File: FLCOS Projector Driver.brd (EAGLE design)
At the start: 73.9 x 62.1 mm, 65 parts, among them IC2 LM3414, IC3 MIC5219BM5, IC4 MIC5219BM5, IC5 LM3414, IC6 LM3414, Q1 14.31818MHz, Q3 12MHz, T2 S8050, T3 S8050, U1 TVP5150-NTSC_DECODER, U2 ESP32-WROOM-32U, U9 CH340G, X1 FH12-25S-0.5SH

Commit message: Updated README
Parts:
- removed JP2: (no value), pinhead:1X03
- added CVBS: (no value), pinhead:1X03
- moved C2 0.09 mm to (70.4, 11.3)
- moved C47 0.08 mm to (22.1, 31.8)
- moved R4 0.05 mm to (70.4, 15.1)
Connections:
- net GND: now also CVBS.3; no longer JP2.3
- net N$20: now also CVBS.1; no longer JP2.1
- net N$21: now also CVBS.2; no longer JP2.2
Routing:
- net +5V: track 194.0 -> 190.3 mm
- net SPI_MOSI: track 61.8 -> 59.3 mm
- net GND: track 74.0 -> 75.2 mm, vias 69 -> 70
- net N$21: track 10.2 -> 10.9 mm
- net N$20: track 13.7 -> 14.4 mm
- net ESP_TX: track 49.2 -> 49.8 mm
- net ESP_RX: track 49.9 -> 50.5 mm
- net SPI_SCLK: track 63.6 -> 63.0 mm
- net N$79: track 12.2 -> 11.6 mm

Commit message: Started BOM. Changing parts to Mouser in-stock
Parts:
- removed Q1: 14.31818MHz, crystal:CTS406
- removed T3: S8050, transistor:SOT23
- removed U$10: MICROSD, micro-sd:C12075
- removed U1: TVP5150-NTSC_DECODER, SparkFun-AnalogIC:TQFP32-5MM
- removed U2: ESP32-WROOM-32U, ESP32-WROOM-32U:ESP32WROOM32D
- removed U9: CH340G, usb-serial:SOIC16
- added FPC: FH12-25S-0.5SH, con-hirose:FH12-25S-0.5SH
- added IC7, IC8, IC9: LM3414, A_butts:SO08-PAD
- added J1: MEM2075-00-140-01-A, MEM2075-00-140-01-A:GCT_MEM2075-00-140-01-A
- added T1: S8050, transistor:SOT23
- C47, C56: value 0.1uF -> 100nF
- IC1: value (none) -> LM1117MPX-3.3
- IC2: value LM3414 -> MIC5219BM5; device A_butts:SO08-PAD -> v-reg-micrel:SOT23-5
- IC4: value MIC5219BM5 -> TVP5150-NTSC_DECODER; device v-reg-micrel:SOT23-5 -> SparkFun-AnalogIC:TQFP32-5MM
- IC5: value LM3414 -> CH340G; device A_butts:SO08-PAD -> usb-serial:SOIC16
- IC6: value LM3414 -> ESP32-WROOM-32U; device A_butts:SO08-PAD -> ESP32-WROOM-32U:ESP32WROOM32D
- L1, L2, L5: value 15uF -> 15uH
- R67: value 4K7 -> 2K2
- X1: value FH12-25S-0.5SH -> 14.31818MHz; device con-hirose:FH12-25S-0.5SH -> crystal:CTS406
- moved IC6 53.1 mm to (18.0, 46.9)
- moved IC5 38.2 mm to (26.4, 15.5), turned to 0 degrees
- moved X1 16.5 mm to (50.1, 60.9), turned to 0 degrees
- moved IC2 16.3 mm to (55.4, 43.7), turned to 0 degrees
- moved IC4 12.7 mm to (50.7, 51.9), turned to 270 degrees
- moved IC3 10.5 mm to (45.5, 40.3)
- moved T2 7.43 mm to (30.6, 23.9), turned to 270 degrees
- moved USB 0.38 mm to (9.60, 14.7)
- moved C47 0.27 mm to (22.3, 31.6)
- moved C55 0.15 mm to (26.5, 37.1)
- moved IC1 0.15 mm to (29.4, 30.7)
- renumbered D5 to D3, Q3 to X2
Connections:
- removed net N$1 (its old number): IC4.4
- new net N$16: IC2.4
- net +1V8: now also IC2.5, IC4.20, IC4.32, IC4.4; no longer IC3.5, U1.20, U1.32, U1.4
- net +2V5: now also FPC.25, IC3.5; no longer IC4.5, X1.25
- net +3V3: now also IC4.10, IC4.28, IC6.2, J1.P4; no longer U$10.4, U1.10, U1.28, U2.2
- net +5V: now also FPC.1, FPC.11, IC2.1, IC2.3, IC5.16, IC7.8, IC8.8, IC9.8; no longer IC2.8, IC4.1, IC4.3, IC5.8, IC6.8, U9.16, X1.1, X1.11
- net AIP1A: now also IC4.1; no longer U1.1
- net AIP1B: now also IC4.2; no longer U1.2
- net BLU_PWM: now also FPC.14, IC9.6; no longer IC5.6, X1.14
- net ESP_EN_N: now also FPC.23, IC6.3, T2.3; no longer T3.3, U2.3, X1.23
- net ESP_RX: now also IC6.34; no longer U2.34
- net ESP_TX: now also IC6.35; no longer U2.35
- net FLCOS_CS_N: now also FPC.3, IC6.26; no longer U2.26, X1.3
- net FLCOS_D0: now also FPC.18, IC4.18, IC6.12; no longer U1.18, U2.12, X1.18
- net FLCOS_D1: now also FPC.17, IC4.17, IC6.13; no longer U1.17, U2.13, X1.17
- net FLCOS_D2: now also FPC.16, IC4.16, IC6.14; no longer U1.16, U2.14, X1.16
- net FLCOS_D3: now also FPC.15, IC4.15, IC6.16; no longer U1.15, U2.16, X1.15
- net FLCOS_D4: now also FPC.10, IC4.14, IC6.36; no longer U1.14, U2.36, X1.10
- net FLCOS_D5: now also FPC.9, IC4.13, IC6.33; no longer U1.13, U2.33, X1.9
- net FLCOS_D6: now also FPC.8, IC4.12, IC6.28; no longer U1.12, U2.28, X1.8
- net FLCOS_D7: now also FPC.7, IC4.11, IC6.27; no longer U1.11, U2.27, X1.7
- net FLCOS_HD: now also FPC.21, IC4.25, IC6.9; no longer U1.25, U2.9, X1.21
- net FLCOS_PCLK: now also FPC.22, IC4.9, IC6.8; no longer U1.9, U2.8, X1.22
- net FLCOS_SOUT: now also FPC.5; no longer X1.5
- net FLCOS_VALID: now also FPC.19, IC4.26, IC6.11; no longer U1.26, U2.11, X1.19
- net FLCOS_VD: now also FPC.20, IC4.24, IC6.10; no longer U1.24, U2.10, X1.20
- net GND: now also FPC.2, FPC.24, IC4.19, IC4.3, IC4.31, IC4.7, IC5.1, IC6.1, IC6.15, IC6.38, IC6.39, IC7.2, IC7.4, IC7.EPAD, IC8.2, IC8.4, IC8.EPAD, IC9.2, IC9.4, IC9.EPAD, J1.P6, J1.SH1, J1.SH2, J1.SH3, J1.SH4; no longer IC2.4, IC2.EPAD, IC4.2, IC5.2, IC5.4, IC5.EPAD, IC6.2, IC6.4, IC6.EPAD, U$10.6, U$10.GND@1, U$10.GND@2, U$10.GND@3, U$10.GND@4, U1.19, U1.3, U1.31, U1.7, U2.1, U2.15, U2.38, U2.39, U9.1, X1.2, X1.24
- net GRN_PWM: now also FPC.13, IC8.6; no longer IC6.6, X1.13
- net N$2: now also IC7.3; no longer IC2.3
- net N$24: now also IC8.3; no longer IC6.3
- net N$25: now also IC8.5; no longer IC6.5
- net N$26: now also IC8.1; no longer IC6.1
- net N$27: now also IC8.7; no longer IC6.7
- net N$3: now also IC7.5; no longer IC2.5
- net N$4: now also IC7.1; no longer IC2.1
- net N$5: now also IC7.7; no longer IC2.7
- net N$6: now also IC9.3; no longer IC5.3
- net N$67: now also IC5.2; no longer U9.2
- net N$7: now also IC9.5; no longer IC5.5
- net N$70: now also IC5.3; no longer U9.3
- net N$71: now also T1.1; no longer T2.1
- net N$77: now also T2.1; no longer T3.1
- net N$78: now also IC5.14, T2.2; no longer T3.2, U9.14
- net N$79: now also IC5.13, T1.2; no longer T2.2, U9.13
- net N$8: now also IC9.1; no longer IC5.1
- net N$80: now also IC5.4; no longer U9.4
- net N$81: now also IC5.7; no longer U9.7
- net N$82: now also IC5.8; no longer U9.8
- net N$9: now also IC9.7; no longer IC5.7
- net RED_PWM: now also FPC.12, IC7.6; no longer IC2.6, X1.12
- net REFM: now also IC4.30; no longer U1.30
- net REFP: now also IC4.29; no longer U1.29
- net SD_CS_N: now also IC6.29, J1.P2; no longer U$10.2, U2.29
- net SPI_MISO: now also IC6.31, J1.P7; no longer U$10.7, U2.31
- net SPI_MOSI: now also FPC.6, IC6.37, J1.P3; no longer U$10.3, U2.37, X1.6
- net SPI_SCLK: now also FPC.4, IC6.30, J1.P5; no longer U$10.5, U2.30, X1.4
- net TVP_FID: now also IC4.23, IC6.6; no longer U1.23, U2.6
- net TVP_FL_RST_N: now also IC4.8, IC6.25, T1.3; no longer T2.3, U1.8, U2.25
- net TVP_INT: now also IC4.27, IC6.7; no longer U1.27, U2.7
- net TVP_SCL: now also IC4.21, IC6.23; no longer U1.21, U2.23
- net TVP_SDA: now also IC4.22, IC6.24; no longer U1.22, U2.24
- net USB_D+: now also IC5.5; no longer U9.5
- net USB_D-: now also IC5.6; no longer U9.6
- net XTAL1: now also IC4.5, X1.3; no longer Q1.3, U1.5
- net XTAL2: now also IC4.6, X1.1; no longer Q1.1, U1.6
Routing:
- net SD_CS_N: track 36.3 -> 39.9 mm
- net SPI_SCLK: track 63.0 -> 66.3 mm, vias 2 -> 4
- net SPI_MOSI: track 59.3 -> 61.2 mm, vias 2 -> 4
- net ESP_TX: track 49.8 -> 48.2 mm
- net ESP_RX: track 50.5 -> 49.0 mm
- net SPI_MISO: track 40.7 -> 41.9 mm
- net TVP_FL_RST_N: track 91.7 -> 92.8 mm
- net +3V3: track 108.6 -> 107.7 mm
- net GND: track 75.2 -> 75.8 mm
- net +5V: track 190.3 -> 189.7 mm

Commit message: ERC and DRC passed. BOM not quite done
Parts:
- removed L5: 15uH, A_butts:TAIYO-YUDEN-6X6X2.8
- added C3: 100nF, rcl:C0603
- added L3: 15uH, A_butts:TAIYO-YUDEN-6X6X2.8
- C14, C15: value 10pF -> 22pF
- D1, D2, D3: value (none) -> "SB34AFC-AU_R1_000A1 SB34AFC-AU_R1_000A1"
- IC2: value MIC5219BM5 -> MIC5323-1.8YD5-TR
- IC3: value MIC5219BM5 -> MIC5504-2.5YM5-TR
- R11: value 0R -> 37R5
- moved L2 9.04 mm to (54.2, 21.4)
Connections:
- removed net N$1: IC3.4
- removed net N$16: IC2.4
- new net N$10: C3.1, IC2.4
- net BLU_CATHODE: now also L3.2; no longer L2.2
- net ESP_EN_N: no longer FPC.23
- net GND: now also C3.2
- net GRN_CATHODE: now also L2.2; no longer L5.2
- net N$27: now also L2.1; no longer L5.1
- net N$9: now also L3.1; no longer L2.1
- net TVP_FL_RST_N: now also FPC.23
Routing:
- net TVP_FL_RST_N: track 92.8 -> 111.9 mm, vias 6 -> 7
- net TVP_FID: track 66.1 -> 58.5 mm
- net ESP_EN_N: track 50.7 -> 44.7 mm
- net +5V: track 189.7 -> 186.6 mm
- net N$10: track 0.00 -> 2.31 mm
- net TVP_INT: track 68.6 -> 66.8 mm, vias 3 -> 5
- net GND: track 75.8 -> 74.5 mm, vias 70 -> 69

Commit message: Changed to USB-C. BOM passives not done yet
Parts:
- removed USB: MINI-USB-32005-301, con-cypressindustries:32005-301
- added R13, R14: 22K, rcl:R0603
- added USB-C: USB4105-GF-A, USB4105-GF-A:GCT_USB4105-GF-A
- R16, R2, R4: value 20K -> 22K
- moved R62 0.38 mm to (18.7, 11.0)
- moved R63 0.38 mm to (18.7, 8.69)
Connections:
- new net CC1: R14.1, USB-C.A5
- new net CC2: R13.1, USB-C.B5
- net +5V: now also R13.2, R14.2, USB-C.A4_B9, USB-C.B4_A9; no longer USB.1
- net GND: now also USB-C.A1_B12, USB-C.B1_A12, USB-C.S1, USB-C.S2, USB-C.S3, USB-C.S4; no longer USB.5
- net USB_D+: now also USB-C.A6, USB-C.B6; no longer USB.3
- net USB_D-: now also USB-C.A7, USB-C.B7; no longer USB.2
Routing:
- net +5V: track 186.6 -> 200.8 mm, vias 7 -> 9
- net CC1: track 0.00 -> 7.63 mm, vias 0 -> 2
- net ESP_RX: track 49.0 -> 42.7 mm
- net CC2: track 0.00 -> 5.37 mm
- net ESP_TX: track 48.2 -> 43.5 mm
- net USB_D-: track 19.1 -> 23.1 mm
- net GND: track 74.5 -> 70.5 mm, vias 69 -> 67
- net USB_D+: track 18.2 -> 21.4 mm

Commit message: Changed Composite pin header for TRRS socket
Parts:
- CVBS: value (none) -> AUDIO_JACK_TRRSSMD_RA; device pinhead:1X03 -> SparkFun-Connectors:AUDIO_JACK_3.5MM_TRRS_SMD_RA
- R1, R15, R3: value 80k -> 80K; device A_butts:R0603 -> rcl:R0603
- R16, R2, R4: device A_butts:R0603 -> rcl:R0603
- moved R3 9.10 mm to (62.6, 25.7)
- moved R16 9.09 mm to (70.4, 15.0)
- moved R15 9.09 mm to (62.6, 16.6)
- moved R4 8.86 mm to (70.4, 24.0)
- moved CVBS 1.41 mm to (68.5, 64.5), turned to 270 degrees
- moved R2 0.21 mm to (70.4, 32.8)
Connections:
- net GND: now also CVBS.EARTH; no longer CVBS.3
- net N$20: now also CVBS.TIP; no longer CVBS.1
- net N$21: now also CVBS.RING2; no longer CVBS.2
- net N$24: now also R4.2; no longer R16.2
- net N$25: now also R3.2; no longer R15.2
- net N$6: now also R16.2; no longer R4.2
- net N$7: now also R15.2; no longer R3.2
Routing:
- net GND: track 70.5 -> 66.3 mm, vias 67 -> 64
- net N$20: track 14.4 -> 10.3 mm

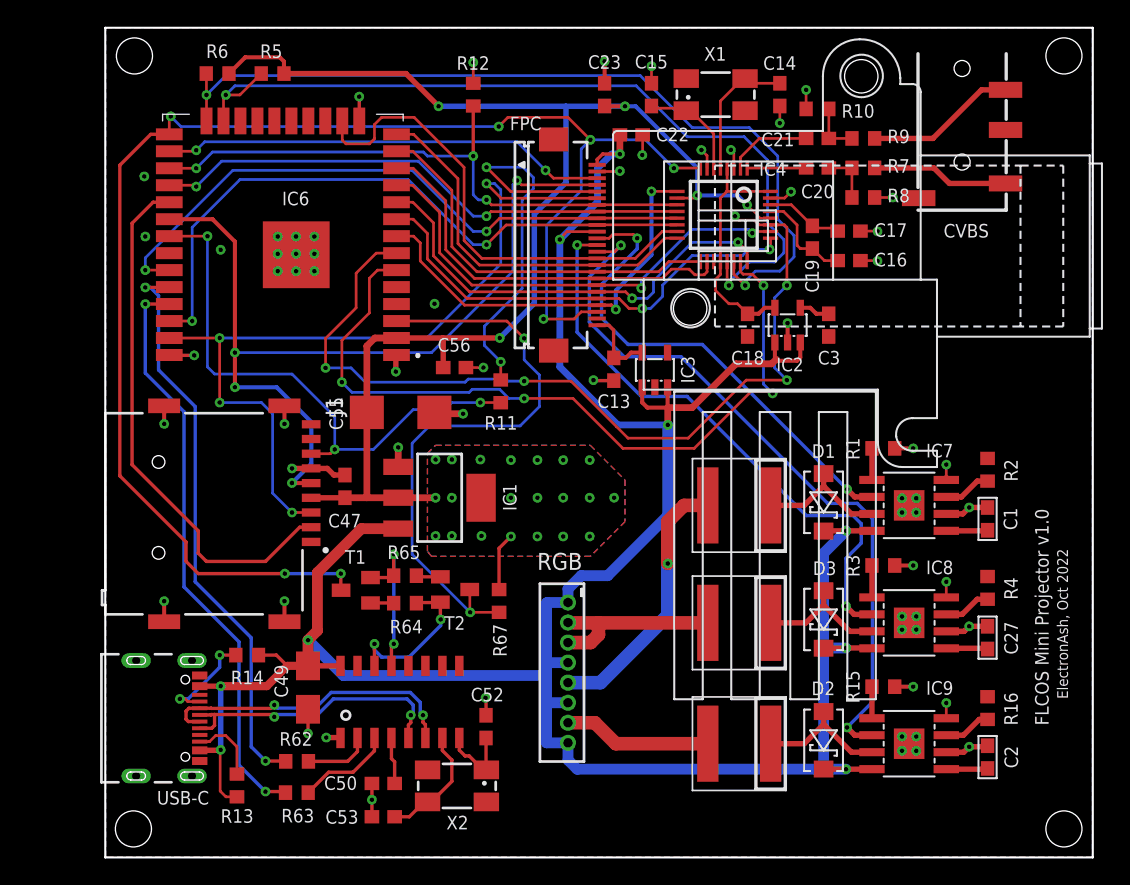
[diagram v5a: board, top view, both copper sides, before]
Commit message: Fixed FLCOS mounting hole position vs flex
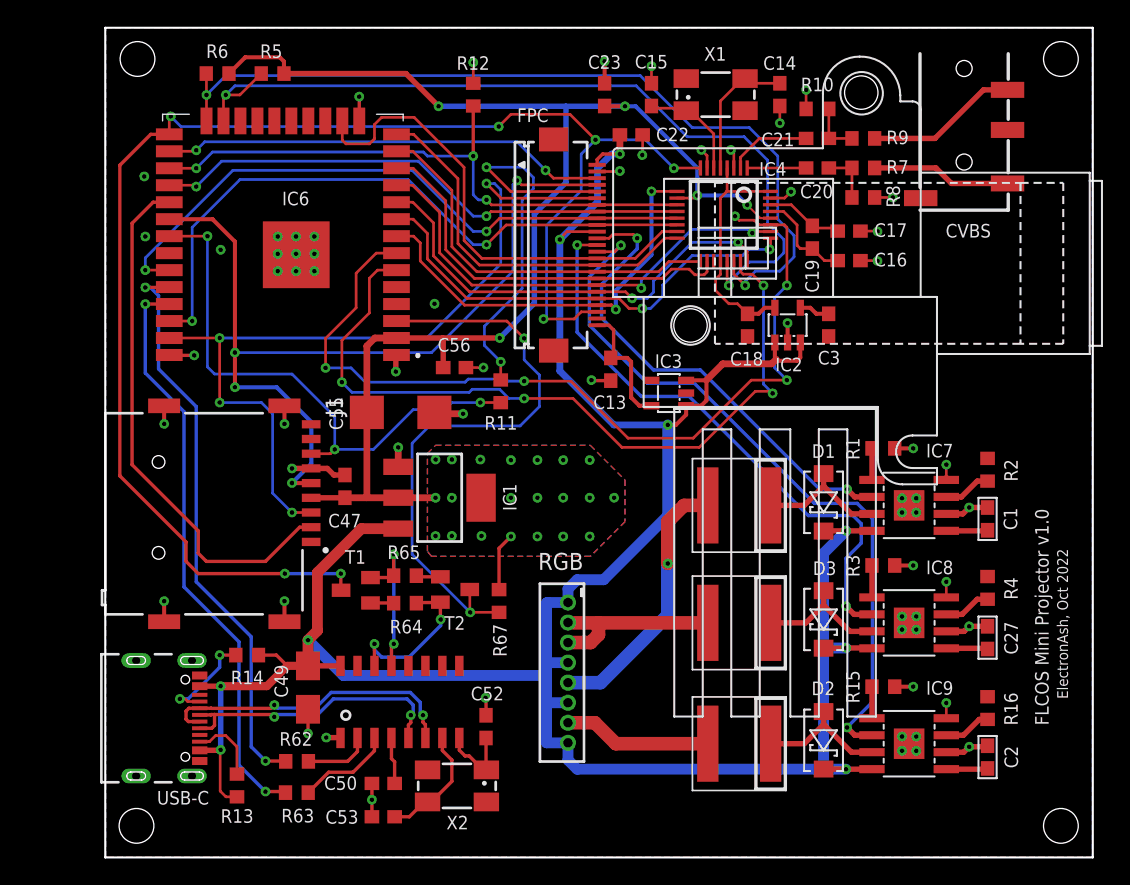
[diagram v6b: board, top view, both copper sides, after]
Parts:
- moved IC3 2.02 mm to (46.6, 38.6), turned to 90 degrees
- moved U$2 1.30 mm to (74.4, 48.6)
- moved C13 0.23 mm to (42.2, 40.4)
- moved CVBS 0.15 mm to (68.7, 64.5)
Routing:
- net +2V5: track 5.79 -> 9.64 mm
- net +5V: track 200.8 -> 198.3 mm

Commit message: Proto PCBs and stencil ordered. Passives BOM not done
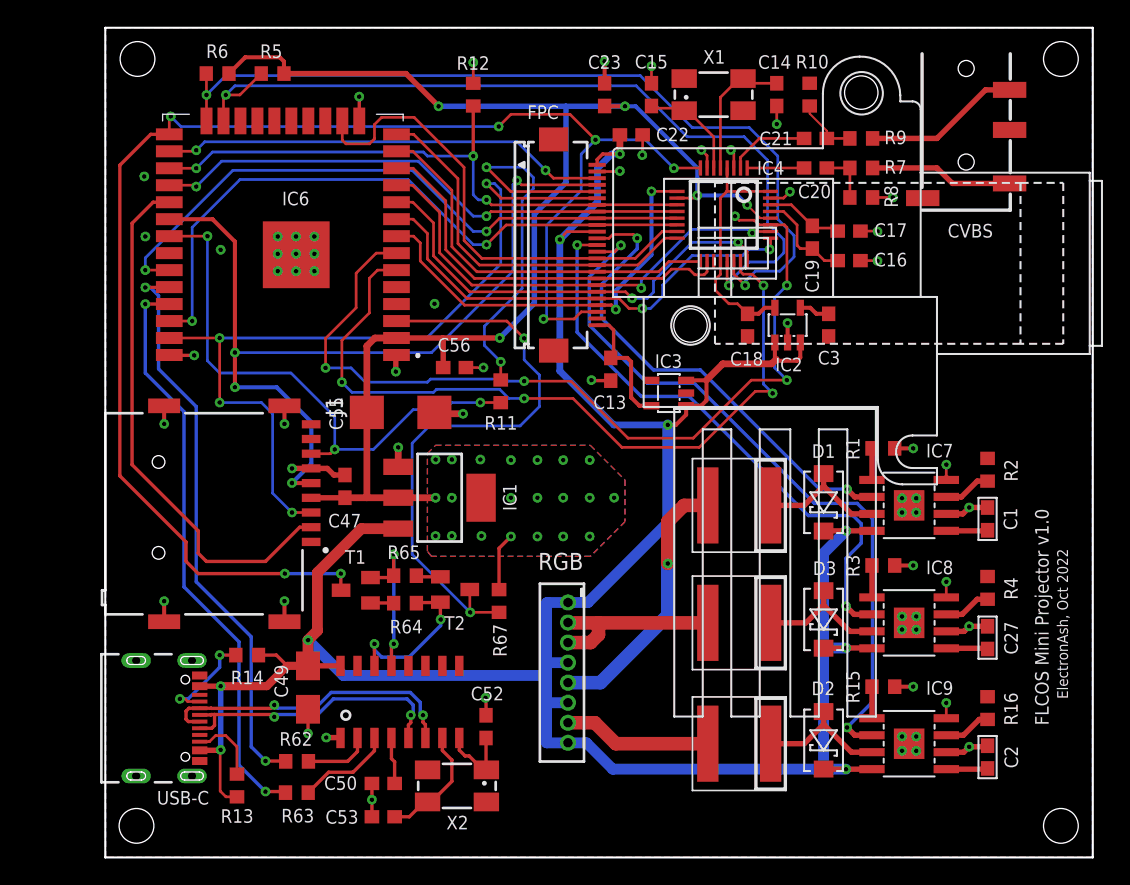
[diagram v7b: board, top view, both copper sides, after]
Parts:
- moved R10 1.22 mm to (57.1, 60.9), turned to 270 degrees
- moved C14 0.23 mm to (54.6, 60.9)
- moved C20 0.15 mm to (57.5, 55.4)
- moved C21 0.15 mm to (57.5, 57.6)
- moved CVBS 0.15 mm to (68.8, 64.5)
- moved R7 0.15 mm to (61.0, 55.4)
- moved R8 0.15 mm to (61.0, 53.2)
- moved R9 0.15 mm to (61.0, 57.6)
- moved X1 0.15 mm to (49.9, 60.9)
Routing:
- net GND: track 66.2 -> 64.9 mm, vias 64 -> 63
- net +5V: track 198.3 -> 197.3 mm
- net N$15: track 3.94 -> 4.69 mm

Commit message: XLSX BOM finished. Tweaked FLCOS mounting points
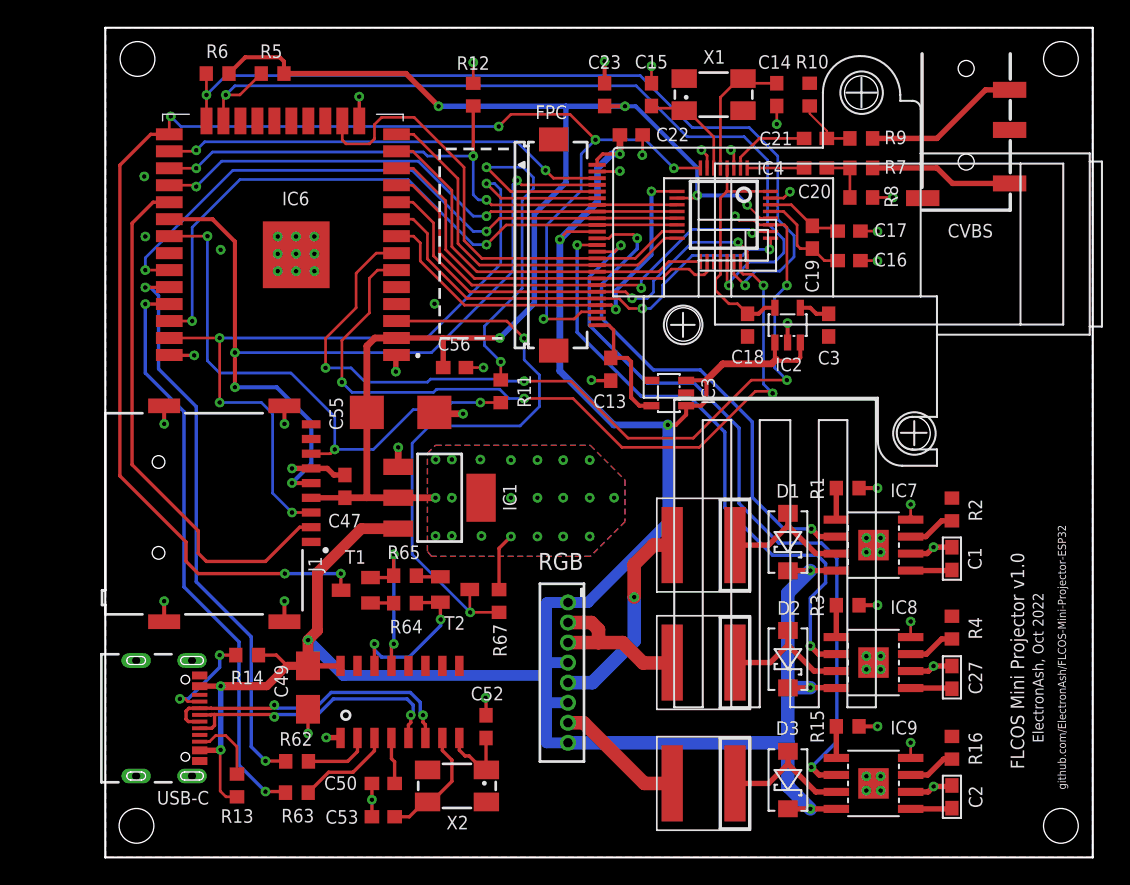
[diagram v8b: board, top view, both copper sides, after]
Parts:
- R1, R15, R3: value 80K -> 82K
- R10, R11, R7, R8, R9: value 37R5 -> 37R4
- moved D3 12.3 mm to (55.5, 9.63)
- moved D2 6.63 mm to (55.5, 18.7)
- moved D1 3.99 mm to (55.5, 27.4)
- moved R4 3.99 mm to (67.7, 21.0)
- moved C2 3.99 mm to (67.7, 8.37)
- moved R16 3.99 mm to (67.7, 12.0)
- moved C1 3.99 mm to (67.7, 26.2)
- moved C27 3.99 mm to (67.7, 17.3)
- moved R2 3.99 mm to (67.7, 29.9)
- moved IC7 3.99 mm to (61.9, 27.2)
- moved IC8 3.99 mm to (61.9, 18.4)
- moved L1 3.99 mm to (51.5, 27.2)
- moved L2 3.99 mm to (51.5, 18.4)
- moved R3 3.99 mm to (59.9, 22.7)
- moved IC9 3.99 mm to (61.9, 9.37)
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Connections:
- net N$27: now also D2.A; no longer D3.A
- net N$9: now also D3.A; no longer D2.A
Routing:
- net RED_CATHODE: track 20.1 -> 15.4 mm
- net +5V: track 197.3 -> 192.8 mm
- net GRN_CATHODE: track 13.9 -> 11.9 mm
- net RED_PWM: track 36.1 -> 37.9 mm
- net GRN_PWM: track 44.1 -> 45.9 mm
- net BLU_PWM: track 54.6 -> 56.5 mm
- net BLU_CATHODE: track 11.1 -> 9.68 mm
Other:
- board text added: "github.com/ElectronAsh/FLCOS-Mini-Projector-ESP32"
